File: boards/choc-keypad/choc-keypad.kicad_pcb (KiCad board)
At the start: 2 copper layers, 95.5 x 127.5 mm, 146 parts, among them J1 Conn_01x08, J2 Conn_01x08, J3 Conn_01x08, J4 Conn_01x08, J5 Conn_01x08, J6 Conn_01x02, J7 Conn_02x06_Odd_Even, J8 Conn_01x06, SW1 Choc, SW10 Choc, SW11 Choc, SW12 Choc, SW13 Choc, SW14 Choc, SW15 Choc, SW16 Choc, SW17 Choc, SW18 Choc, SW19 Choc, SW2 Choc, SW20 Choc, SW21 Choc, SW22 Choc, SW23 Choc, SW24 Choc, SW3 Choc, SW4 Choc, SW5 Choc, SW6 Choc, SW7 Choc, SW8 Choc, SW9 Choc

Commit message: Finalize choc-keypad
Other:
- board text added: "1"
- board text added: "2"
- board text added: "3"
- board text added: "4"
- board text added: "5"
- board text added: "6"
- board text added: "@bitshiftmask"
- board text added: "COL"
- board text added: "DI"
- board text added: "DO"
- board text added: "GND"
- board text added: "ROW"
- board text added: "VCC"
- board text added: "brick-mount keypad"
- board text added: "don't look at my butt."
- board text added: "v0.1.0 - Jan. 2021"

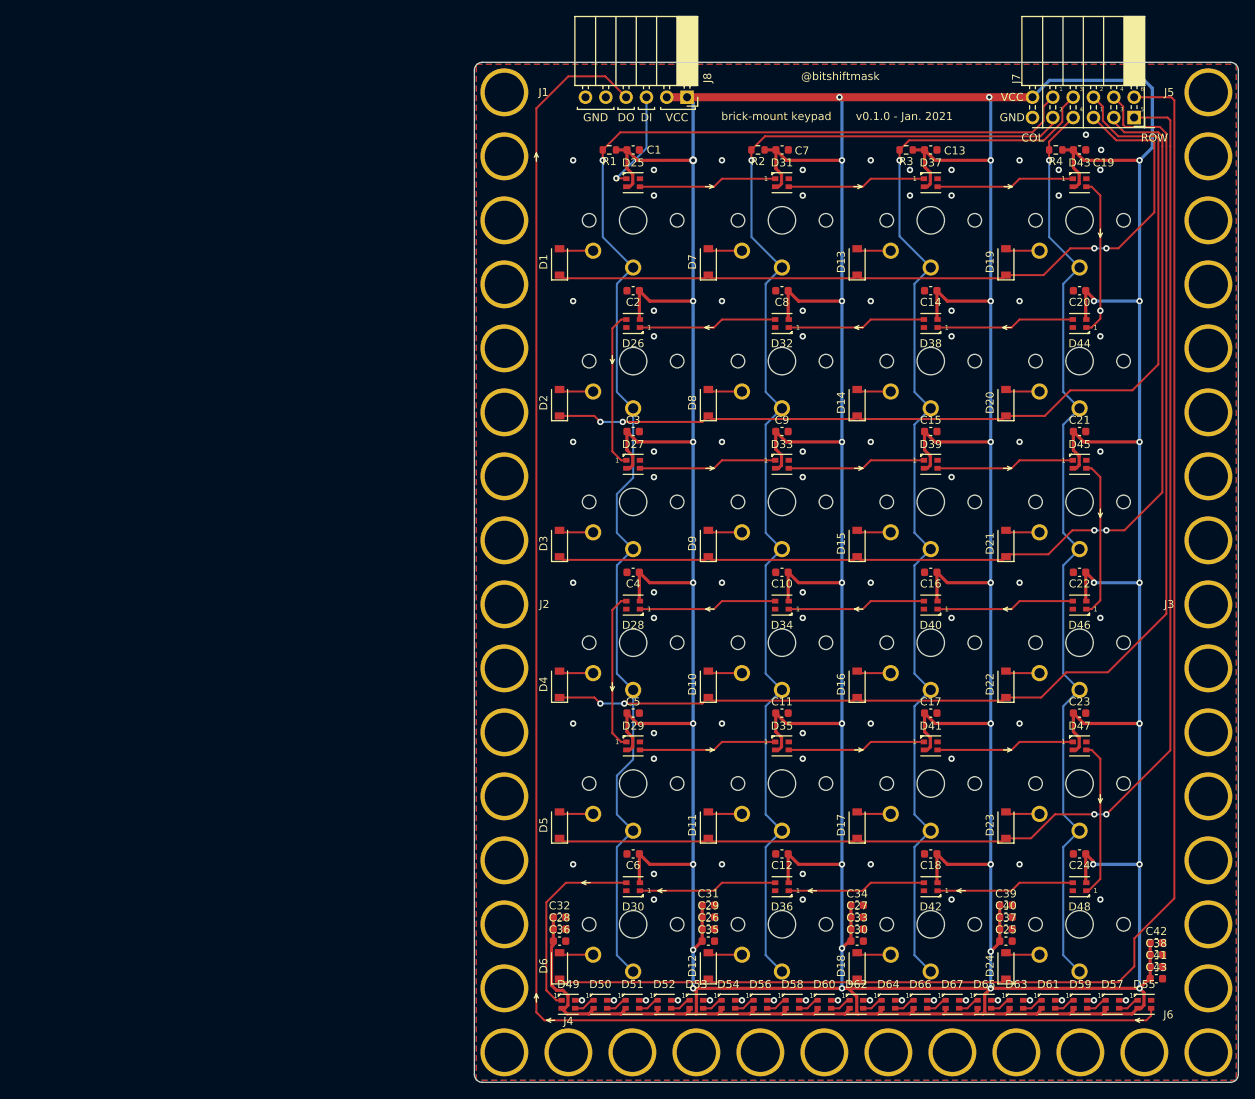
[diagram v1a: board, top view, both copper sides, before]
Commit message: Fix some silkscreen, update to v0.1.1 for non-X2 re-export
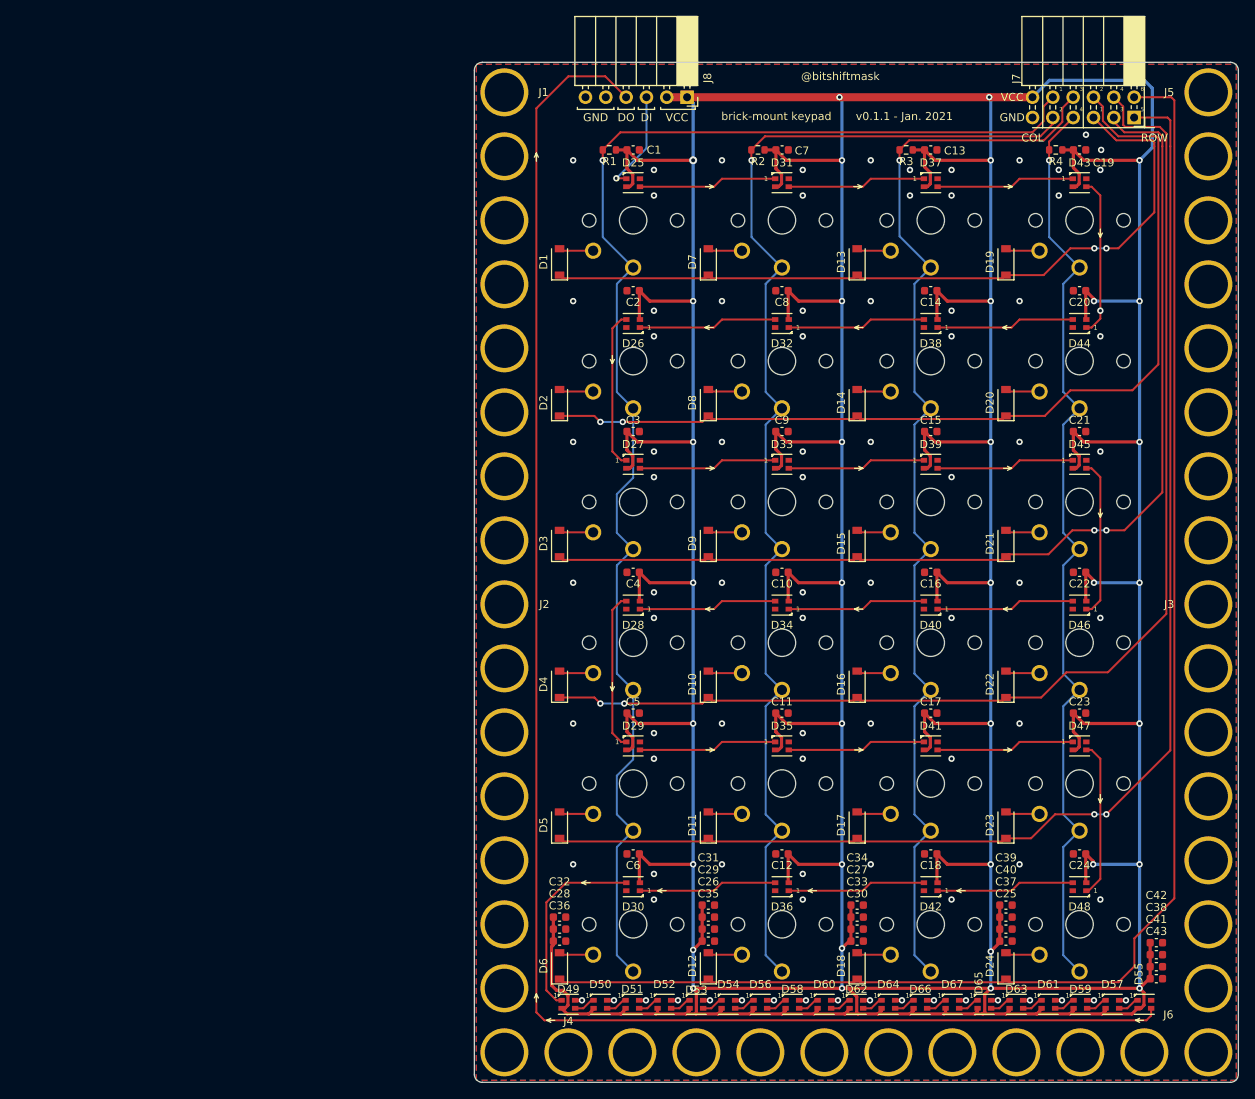
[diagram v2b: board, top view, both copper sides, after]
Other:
- board text added: "v0.1.1 - Jan. 2021"
- board text removed: "v0.1.0 - Jan. 2021"

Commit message: Pre-stream setup
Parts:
- added REF**: SW_Cherry_MX_1.00u_PCB, Button_Switch_Keyboard:SW_Cherry_MX_1.00u_PCB, F.Cu at (42.5, 74.9)
- added SW55: Choc, keyswitches:PG1350, F.Cu at (40.0, 80.0)
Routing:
- net Net-(D43-Pad3): vias 1 -> 0
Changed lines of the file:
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@@
     (thickness 1.6)
     (drawings 145)
-    (tracks 844)
+    (tracks 843)
     (zones 0)
-    (modules 146)
+    (modules 148)
     (nets 81)
   )
@@
     (mod_text_size 1 1)
     (mod_text_width 0.15)
-    (pad_size 1.524 1.524)
-    (pad_drill 0.762)
+    (pad_size 4 4)
+    (pad_drill 4)
     (pad_to_mask_clearance 0)
     (aux_axis_origin 0 0)
@@
     (add_net VCC)
   )
+  (module Button_Switch_Keyboard:SW_Cherry_MX_1.00u_PCB (layer F.Cu)
+    (at 42.54 74.92)
+    (descr "Cherry MX keyswitch, 1.00u, PCB mount, http://cherryamericas.com/wp-content/uploads/2014/12/mx_cat.pdf")
+    (tags "Cherry MX keyswitch 1.00u PCB")
+    (fp_text reference REF** (at -2.54 -2.794) (layer F.SilkS)
+      (effects (font (size 1 1) (thickness 0.15)))
+    )
+    (fp_text value SW_Cherry_MX_1.00u_PCB (at -2.54 12.954) (layer F.Fab)
+      (effects (font (size 1 1) (thickness 0.15)))
+    )
+    (fp_line (start -8.89 -1.27) (end 3.81 -1.27) (layer F.Fab) (width 0.1))
+    (fp_line (start 3.81 -1.27) (end 3.81 11.43) (layer F.Fab) (width 0.1))
+    (fp_line (start 3.81 11.43) (end -8.89 11.43) (layer F.Fab) (width 0.1))
+    (fp_line (start -8.89 11.43) (end -8.89 -1.27) (layer F.Fab) (width 0.1))
+    (fp_line (start -9.14 11.68) (end -9.14 -1.52) (layer F.CrtYd) (width 0.05))
+    (fp_line (start 4.06 11.68) (end -9.14 11.68) (layer F.CrtYd) (width 0.05))
+    (fp_line (start 4.06 -1.52) (end 4.06 11.68) (layer F.CrtYd) (width 0.05))
+    (fp_line (start -9.14 -1.52) (end 4.06 -1.52) (layer F.CrtYd) (width 0.05))
+    (fp_line (start -12.065 -4.445) (end 6.985 -4.445) (layer Dwgs.User) (width 0.15))
+    (fp_line (start 6.985 -4.445) (end 6.985 14.605) (layer Dwgs.User) (width 0.15))
+    (fp_line (start 6.985 14.605) (end -12.065 14.605) (layer Dwgs.User) (width 0.15))
+    (fp_line (start -12.065 14.605) (end -12.065 -4.445) (layer Dwgs.User) (width 0.15))
+    (fp_line (start -9.525 -1.905) (end 4.445 -1.905) (layer F.SilkS) (width 0.12))
+    (fp_line (start 4.445 -1.905) (end 4.445 12.065) (layer F.SilkS) (width 0.12))
+    (fp_line (start 4.445 12.065) (end -9.525 12.065) (layer F.SilkS) (width 0.12))
+    (fp_line (start -9.525 12.065) (end -9.525 -1.905) (layer F.SilkS) (width 0.12))
+    (fp_text user %R (at -2.54 -2.794) (layer F.Fab)
+      (effects (font (size 1 1) (thickness 0.15)))
+    )
+    (pad 1 thru_hole circle (at 0 0) (size 2.2 2.2) (drill 1.5) (layers *.Cu *.Mask))
+    (pad 2 thru_hole circle (at -6.35 2.54) (size 2.2 2.2) (drill 1.5) (layers *.Cu *.Mask))
+    (pad "" np_thru_hole circle (at -2.54 5.08) (size 4 4) (drill 4) (layers *.Cu *.Mask))
+    (pad "" np_thru_hole circle (at -7.62 5.08) (size 1.7 1.7) (drill 1.7) (layers *.Cu *.Mask))
+    (pad "" np_thru_hole circle (at 2.54 5.08) (size 1.7 1.7) (drill 1.7) (layers *.Cu *.Mask))
+    (model ${KISYS3DMOD}/Button_Switch_Keyboard.3dshapes/SW_Cherry_MX_1.00u_PCB.wrl
+      (at (xyz 0 0 0))
+      (scale (xyz 1 1 1))
+      (rotate (xyz 0 0 0))
+    )
+  )
+  (module keyswitches:PG1350 (layer F.Cu)
+    (at 40 80)
+    (descr "Kailh \"Choc\" PG1350 keyswitch")
+    (tags kailh,choc)
+    (fp_text reference SW55 (at 0 8.3) (layer B.SilkS)
+      (effects (font (size 1 1) (thickness 0.15)) (justify mirror))
+    )
+    (fp_text value Choc (at 0 -8.7) (layer F.Fab)
+      (effects (font (size 1 1) (thickness 0.15)))
+    )
+    (fp_line (start -7.5 7.5) (end -7.5 -7.5) (layer Eco2.User) (width 0.15))
+    (fp_line (start 7.5 7.5) (end -7.5 7.5) (layer Eco2.User) (width 0.15))
+    (fp_line (start 7.5 -7.5) (end 7.5 7.5) (layer Eco2.User) (width 0.15))
+    (fp_line (start -7.5 -7.5) (end 7.5 -7.5) (layer Eco2.User) (width 0.15))
+    (fp_line (start -6.9 6.9) (end -6.9 -6.9) (layer Eco2.User) (width 0.15))
+    (fp_line (start 6.9 -6.9) (end 6.9 6.9) (layer Eco2.User) (width 0.15))
+    (fp_line (start 6.9 -6.9) (end -6.9 -6.9) (layer Eco2.User) (width 0.15))
+    (fp_line (start -6.9 6.9) (end 6.9 6.9) (layer Eco2.User) (width 0.15))
+    (fp_line (start 7 -7) (end 7 -6) (layer B.SilkS) (width 0.15))
+    (fp_line (start 6 -7) (end 7 -7) (layer B.SilkS) (width 0.15))
+    (fp_line (start 7 7) (end 6 7) (layer B.SilkS) (width 0.15))
+    (fp_line (start 7 6) (end 7 7) (layer B.SilkS) (width 0.15))
+    (fp_line (start -7 7) (end -7 6) (layer B.SilkS) (width 0.15))
+    (fp_line (start -6 7) (end -7 7) (layer B.SilkS) (width 0.15))
+    (fp_line (start -7 -7) (end -6 -7) (layer B.SilkS) (width 0.15))
+    (fp_line (start -7 -6) (end -7 -7) (layer B.SilkS) (width 0.15))
+    (fp_line (start -2.6 -3.1) (end -2.6 -6.3) (layer Eco2.User) (width 0.15))
+    (fp_line (start 2.6 -6.3) (end -2.6 -6.3) (layer Eco2.User) (width 0.15))
+    (fp_line (start 2.6 -3.1) (end 2.6 -6.3) (layer Eco2.User) (width 0.15))
+    (fp_line (start -2.6 -3.1) (end 2.6 -3.1) (layer Eco2.User) (width 0.15))
+    (pad "" np_thru_hole circle (at 0 0) (size 3.429 3.429) (drill 3.429) (layers *.Cu *.Mask))
+    (pad 2 thru_hole circle (at -5 3.8) (size 2.032 2.032) (drill 1.27) (layers *.Cu *.Mask))
+    (pad 1 thru_hole circle (at 0 5.9) (size 2.032 2.032) (drill 1.27) (layers *.Cu *.Mask))
+    (pad "" np_thru_hole circle (at 5.5 0) (size 1.7018 1.7018) (drill 1.7018) (layers *.Cu *.Mask))
+    (pad "" np_thru_hole circle (at -5.5 0) (size 1.7018 1.7018) (drill 1.7018) (layers *.Cu *.Mask))
+    (model ${KIPRJMOD}/../../parts/reform/reform2-keyboard-pcb/3d-models/Kailh_keycap-switch_system_1x1.wrl
+      (offset (xyz 0 0 7.1))
+      (scale (xyz 0.4 0.4 0.4))
+      (rotate (xyz -90 0 0))
+    )
+  )
   (module Capacitor_SMD:C_0603_1608Metric (layer F.Cu)
     (at 175.5 164.8)
@@
   (segment (start 168.5 66.9) (end 168.5 81.3) (width 0.25) (layer F.Cu) (net 47))
   (segment (start 168.5 81.3) (end 168.5 82.3) (width 0.25) (layer F.Cu) (net 47))
-  (via (at 168.5 81.3) (size 0.8) (drill 0.4) (layers F.Cu B.Cu) (net 47))
   (segment (start 167.4 118.6) (end 166.75 118.6) (width 0.25) (layer F.Cu) (net 48))
   (segment (start 168.5 117.5) (end 167.4 118.6) (width 0.25) (layer F.Cu) (net 48))
